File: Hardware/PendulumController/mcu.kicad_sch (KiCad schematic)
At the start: 21 parts, among them J201 ICSP, SW201 RESET, SW202 START_SW, SW203 STOP/MODE_SW, U201 ATmega328P, Y201 16mHz

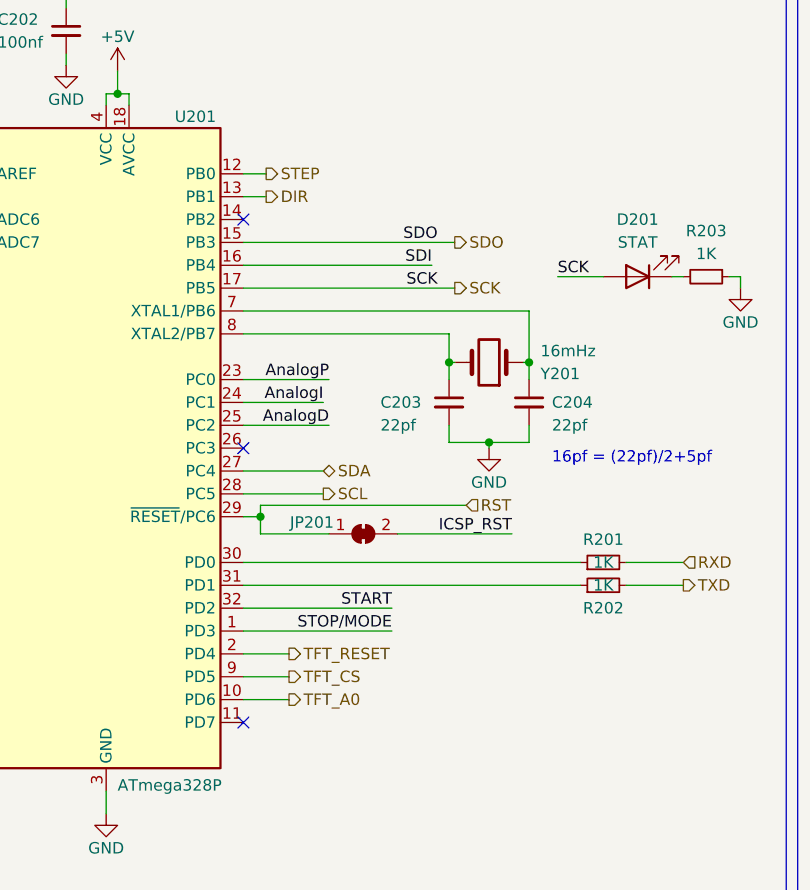
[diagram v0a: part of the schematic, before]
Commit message: Clean up board design with embedded power supply
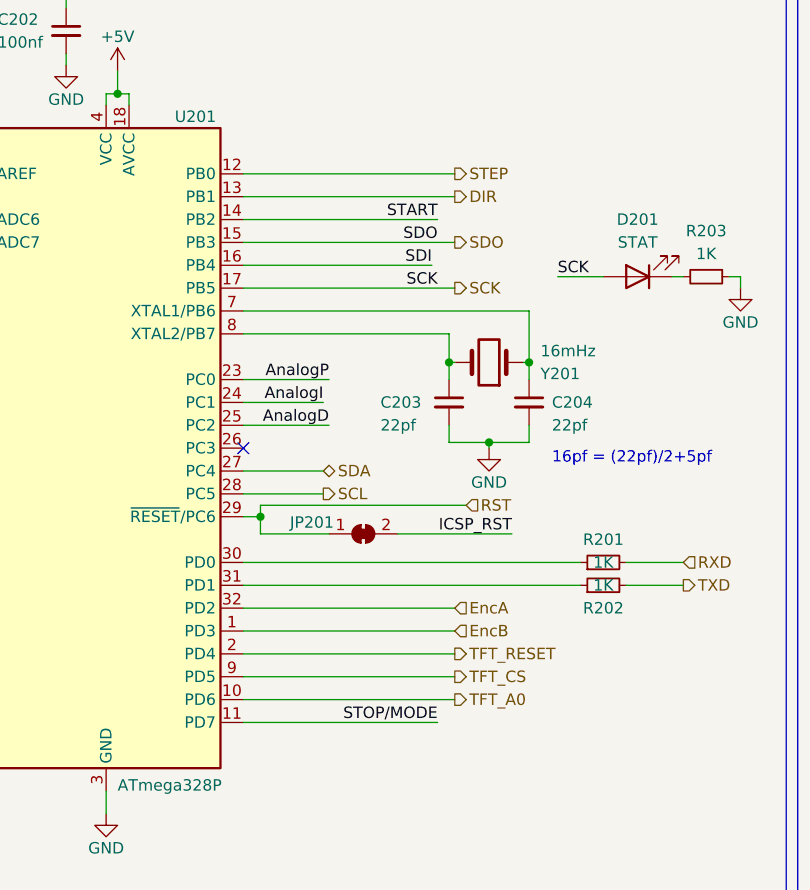
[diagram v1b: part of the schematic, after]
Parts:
- RV201, RV202, RV203: footprint (none) -> Connector_JST:JST_EH_B3B-EH-A_1x03_P2.50mm_Vertical
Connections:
- net START: now also U201.14 (PB2); no longer U201.32 (PD2)
- net STOP/MODE: now also U201.11 (PD7); no longer U201.1 (PD3)
- new net EncA: U201.32 (PD2)
- new net EncB: U201.1 (PD3)
- no-connect marks 9 -> 7
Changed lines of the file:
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@@
   (junction (at 59.69 86.995) (diameter 0) (color 0 0 0 0)
   )
-  (no_connect (at 57.785 79.375))
   (no_connect (at 27.305 56.515))
   (no_connect (at 48.26 154.94))
   (no_connect (at 48.26 157.48))
   (no_connect (at 48.26 152.4))
-  (no_connect (at 57.785 109.855))
   (no_connect (at 35.56 152.4))
+  (no_connect (at 57.785 79.375))
   (no_connect (at 27.305 53.975))
-  (no_connect (at 57.785 53.975))
-  (wire (pts (xy 57.785 48.895) (xy 60.325 48.895))
+  (wire (pts (xy 57.785 48.895) (xy 81.28 48.895))
     (stroke (width 0) (type default) (color 0 0 0 0))
   )
@@
     (stroke (width 0) (type default) (color 0 0 0 0))
   )
-  (wire (pts (xy 57.785 51.435) (xy 60.325 51.435))
+  (wire (pts (xy 57.785 51.435) (xy 81.28 51.435))
     (stroke (width 0) (type default) (color 0 0 0 0))
   )
@@
     (stroke (width 0) (type default) (color 0 0 0 0))
   )
-  (wire (pts (xy 57.785 107.315) (xy 62.865 107.315))
+  (wire (pts (xy 57.785 107.315) (xy 81.28 107.315))
     (stroke (width 0) (type default) (color 0 0 0 0))
   )
@@
     (stroke (width 0) (type default) (color 0 0 0 0))
   )
-  (wire (pts (xy 57.785 102.235) (xy 62.865 102.235))
+  (wire (pts (xy 57.785 102.235) (xy 81.28 102.235))
     (stroke (width 0) (type default) (color 0 0 0 0))
   )
@@
     (stroke (width 0) (type default) (color 0 0 0 0))
   )
+  (wire (pts (xy 79.375 53.975) (xy 57.785 53.975))
+    (stroke (width 0) (type default) (color 0 0 0 0))
+  )
   (wire (pts (xy 187.96 41.91) (xy 187.96 44.45))
     (stroke (width 0) (type default) (color 0 0 0 0))
@@
     (stroke (width 0) (type default) (color 0 0 0 0))
   )
+  (wire (pts (xy 79.375 109.855) (xy 57.785 109.855))
+    (stroke (width 0) (type default) (color 0 0 0 0))
+  )
   (wire (pts (xy 38.1 29.21) (xy 38.1 30.48))
     (stroke (width 0) (type default) (color 0 0 0 0))
   )
-  (wire (pts (xy 74.295 99.695) (xy 57.785 99.695))
+  (wire (pts (xy 81.28 99.695) (xy 57.785 99.695))
     (stroke (width 0) (type default) (color 0 0 0 0))
   )
@@
     (stroke (width 0) (type default) (color 0 0 0 0))
   )
-  (wire (pts (xy 74.295 97.155) (xy 57.785 97.155))
+  (wire (pts (xy 81.28 97.155) (xy 57.785 97.155))
     (stroke (width 0) (type default) (color 0 0 0 0))
   )
@@
     (stroke (width 0) (type default) (color 0 0 0 0))
   )
-  (wire (pts (xy 57.785 104.775) (xy 62.865 104.775))
+  (wire (pts (xy 57.785 104.775) (xy 81.28 104.775))
     (stroke (width 0) (type default) (color 0 0 0 0))
   )
@@
     (effects (font (size 1.27 1.27)) (justify left bottom))
   )
+  (label "START" (at 79.375 53.975 180)
+    (effects (font (size 1.27 1.27)) (justify right bottom))
+  )
   (label "SDI" (at 24.13 160.02 0)
     (effects (font (size 1.27 1.27)) (justify left bottom))
   )
+  (label "STOP{slash}MODE" (at 79.375 109.855 180)
+    (effects (font (size 1.27 1.27)) (justify right bottom))
+  )
   (label "START" (at 154.305 27.305 0)
     (effects (font (size 1.27 1.27)) (justify left bottom))
@@
     (effects (font (size 1.27 1.27)) (justify right bottom))
   )
-  (label "STOP{slash}MODE" (at 74.295 99.695 180)
-    (effects (font (size 1.27 1.27)) (justify right bottom))
-  )
   (label "ICSP_RST" (at 24.13 154.94 0)
     (effects (font (size 1.27 1.27)) (justify left bottom))
@@
   )
   (label "AnalogD" (at 67.31 76.835 180)
-    (effects (font (size 1.27 1.27)) (justify right bottom))
-  )
-  (label "START" (at 74.295 97.155 180)
     (effects (font (size 1.27 1.27)) (justify right bottom))
   )
@@
     (effects (font (size 1.27 1.27)) (justify left))
   )
-  (hierarchical_label "TFT_CS" (shape output) (at 62.865 104.775 0)
+  (hierarchical_label "TFT_CS" (shape output) (at 81.28 104.775 0)
     (effects (font (size 1.27 1.27)) (justify left))
   )
@@
     (effects (font (size 1.27 1.27)) (justify left))
   )
-  (hierarchical_label "TFT_RESET" (shape output) (at 62.865 102.235 0)
-    (effects (font (size 1.27 1.27)) (justify left))
-  )
-  (hierarchical_label "DIR" (shape output) (at 60.325 51.435 0)
+  (hierarchical_label "TFT_RESET" (shape output) (at 81.28 102.235 0)
+    (effects (font (size 1.27 1.27)) (justify left))
+  )
+  (hierarchical_label "EncB" (shape input) (at 81.28 99.695 0)
+    (effects (font (size 1.27 1.27)) (justify left))
+  )
+  (hierarchical_label "DIR" (shape output) (at 81.28 51.435 0)
+    (effects (font (size 1.27 1.27)) (justify left))
+  )
+  (hierarchical_label "EncA" (shape input) (at 81.28 97.155 0)
     (effects (font (size 1.27 1.27)) (justify left))
   )
@@
     (effects (font (size 1.27 1.27)) (justify left))
   )
-  (hierarchical_label "TFT_A0" (shape output) (at 62.865 107.315 0)
+  (hierarchical_label "TFT_A0" (shape output) (at 81.28 107.315 0)
     (effects (font (size 1.27 1.27)) (justify left))
   )
@@
     (effects (font (size 1.27 1.27)) (justify left))
   )
-  (hierarchical_label "STEP" (shape output) (at 60.325 48.895 0)
+  (hierarchical_label "STEP" (shape output) (at 81.28 48.895 0)
     (effects (font (size 1.27 1.27)) (justify left))
   )
@@
       (effects (font (size 1.27 1.27)) (justify right))
     )
-    (property "Footprint" "" (id 2) (at 129.54 57.15 0)
+    (property "Footprint" "Connector_JST:JST_EH_B3B-EH-A_1x03_P2.50mm_Vertical" (id 2) (at 129.54 57.15 0)
       (effects (font (size 1.27 1.27)) hide)
     )
@@
       (effects (font (size 1.27 1.27)) (justify right))
     )
-    (property "Footprint" "" (id 2) (at 129.54 77.47 0)
+    (property "Footprint" "Connector_JST:JST_EH_B3B-EH-A_1x03_P2.50mm_Vertical" (id 2) (at 129.54 77.47 0)
       (effects (font (size 1.27 1.27)) hide)
     )
@@
       (effects (font (size 1.27 1.27)) (justify right))
     )
-    (property "Footprint" "" (id 2) (at 129.54 97.155 0)
-      (effects (font (size 1.27 1.27)) hide)
-    )
+    (property "Footprint" "Connector_JST:JST_EH_B3B-EH-A_1x03_P2.50mm_Vertical" (id 2) (at 129.54 97.155 0)
+      (effects (font (size 1.27 1.27)) hide)
+    )
